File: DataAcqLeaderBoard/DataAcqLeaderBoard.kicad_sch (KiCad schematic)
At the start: 11 parts, among them SW1 UP, U1 PA1616S_GPS

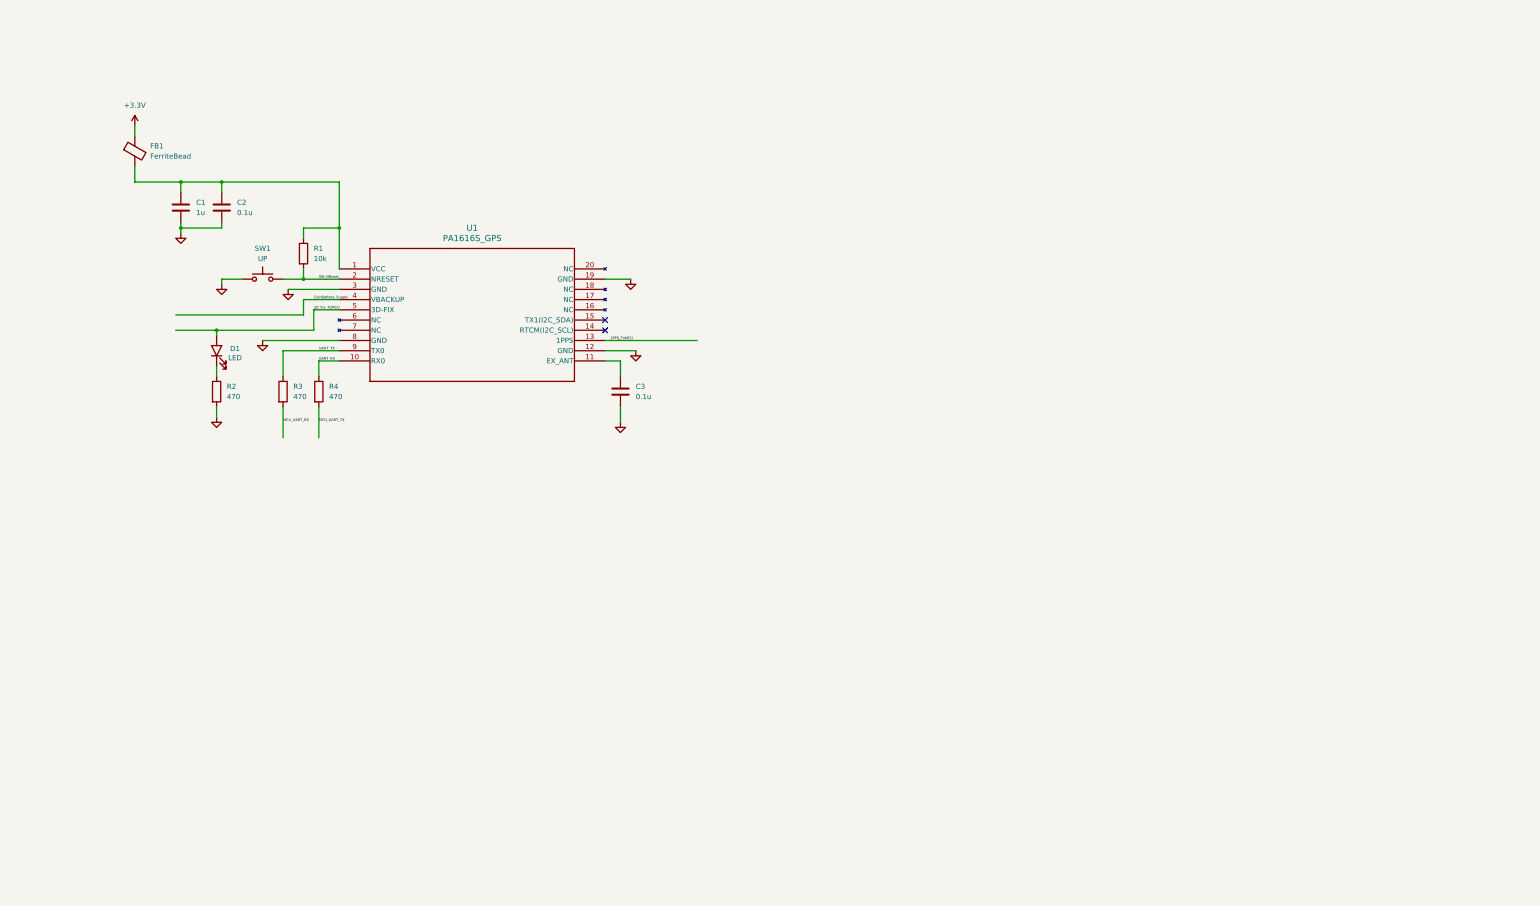
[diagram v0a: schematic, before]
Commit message: Added XBee RF Module
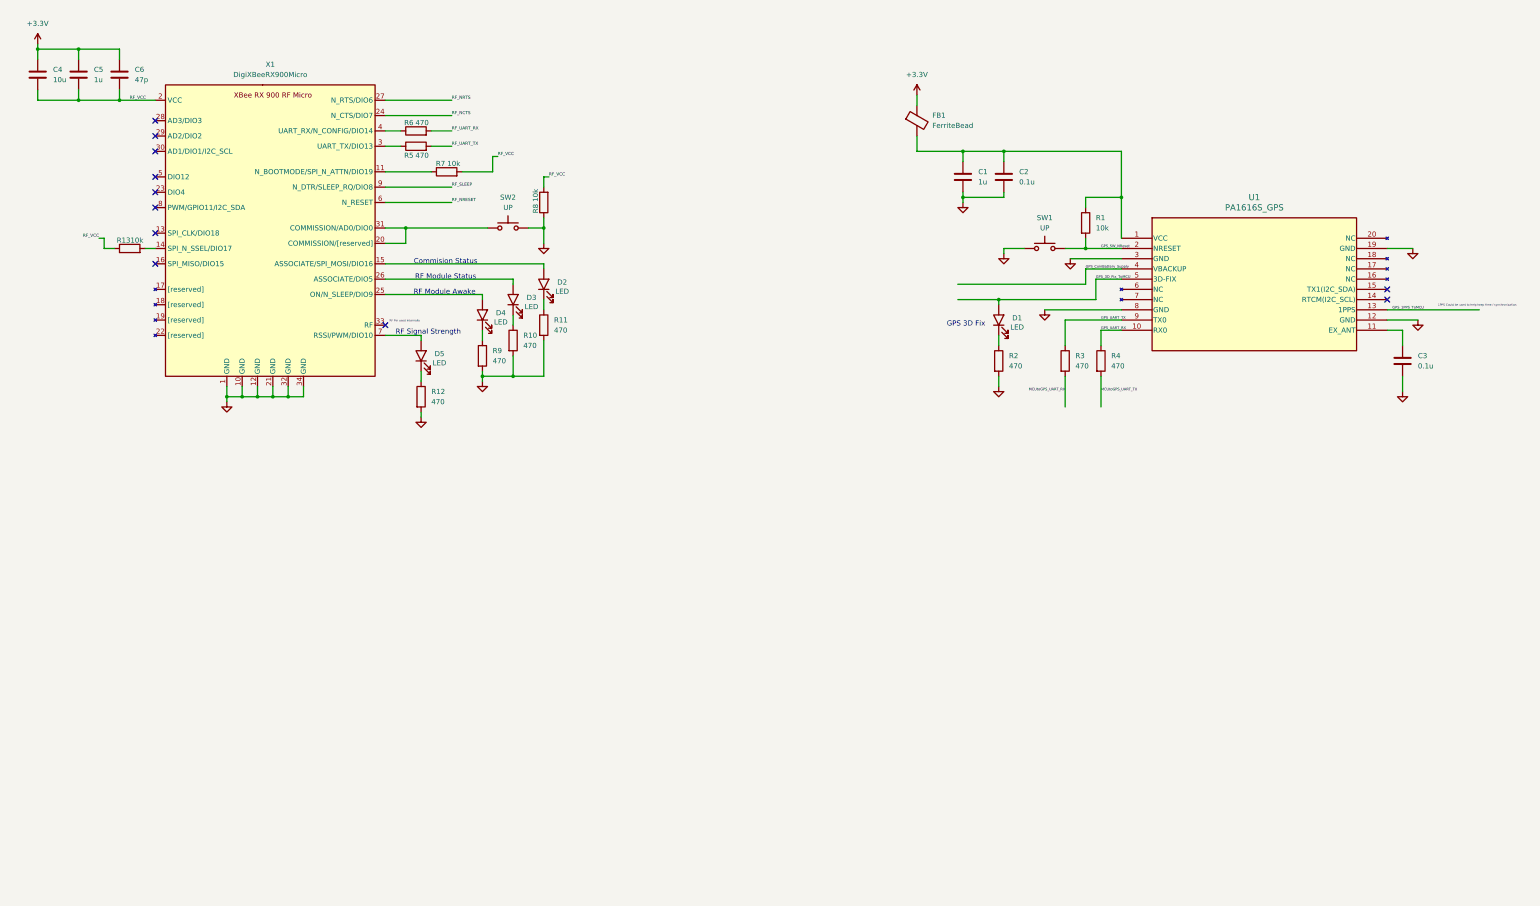
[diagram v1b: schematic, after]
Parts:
- added C4: 10u, ECE319K:C_Axial_200mil, symbol ECE319K:C
- added C5: 1u, ECE319K:C_Axial_200mil, symbol ECE319K:C
- added C6: 47p, ECE319K:C_Axial_200mil, symbol ECE319K:C
- added D2, D3, D4, D5: LED, ECE319K:LED_D5.0mm, symbol ECE319K:LED
- added R10, R11, R12, R5, R6, R9: 470, symbol Device:R
- added R13, R7, R8: 10k, symbol Device:R
- added SW2: UP, ECE319K:SW_PUSH_6mm, symbol ECE319K:SW_Push
- added X1: DigiXBeeRX900Micro, symbol DataAcqLeaderBoard-SchematicSymbols:DigiXBeeRX900Micro
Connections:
- net +3.3V: now also C4.1, C5.1, C6.1
- net GND: now also R10.2, R11.2, R12.2, R8.1, R9.2, SW2.2, X1.1 (GND), X1.10 (GND), X1.12 (GND), X1.21 (GND), X1.32 (GND), X1.34 (GND)
- net 1PPS_ToMCU renamed GPS_1PPS_ToMCU
- net 3D_Fix_ToMCU renamed GPS_3D_Fix_ToMCU
- net CoinBattery_Supply renamed GPS_CoinBattery_Supply
- net MCU_UART_RX renamed MCUtoGPS_UART_RX
- net MCU_UART_TX renamed MCUtoGPS_UART_TX
- net SW_NReset renamed GPS_SW_NReset
- net UART_RX renamed GPS_UART_RX
- net UART_TX renamed GPS_UART_TX
- new net: D2.1 (K), R11.1
- new net: D3.1 (K), R10.1
- new net: D3.2 (A), X1.26 (ASSOCIATE/DIO5)
- new net: D5.1 (K), R12.1
- new net: SW2.1, X1.20 (COMMISSION/[reserved]), X1.31 (COMMISSION/AD0/DIO0)
- new net: R6.1, X1.4 (UART_RX/N_CONFIG/DIO14)
- new net: R7.1, X1.11 (N_BOOTMODE/SPI_N_ATTN/DIO19)
- new net: R13.2, X1.14 (SPI_N_SSEL/DIO17)
- new net: D2.2 (A), X1.15 (ASSOCIATE/SPI_MOSI/DIO16)
- new net: D4.2 (A), X1.25 (ON/N_SLEEP/DIO9)
- new net: R5.1, X1.3 (UART_TX/DIO13)
- new net: D5.2 (A), X1.7 (RSSI/PWM/DIO10)
- new net: D4.1 (K), R9.1
- new net RF_NCTS: X1.24 (N_CTS/DIO7)
- new net RF_NRESET: X1.6 (N_RESET)
- new net RF_NRTS: X1.27 (N_RTS/DIO6)
- new net RF_SLEEP: X1.9 (N_DTR/SLEEP_RQ/DIO8)
- new net RF_UART_RX: R6.2
- new net RF_UART_TX: R5.2
- new net RF_VCC: C4.2, C5.2, C6.2, R13.1, R7.2, R8.2, X1.2 (VCC)
- no-connect marks 2 -> 11
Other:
- note added: "1PPS Could be used to help keep time / synchronization"
- note added: "Commision Status"
- note added: "GPS 3D Fix"
- note added: "RF Module Awake"
- note added: "RF Module Status"
- note added: "RF Pin used internally"
- note added: "RF Signal Strength"
- moved on the sheet: C1, C2, C3, D1, FB1, R1, R2, R3, R4, SW1

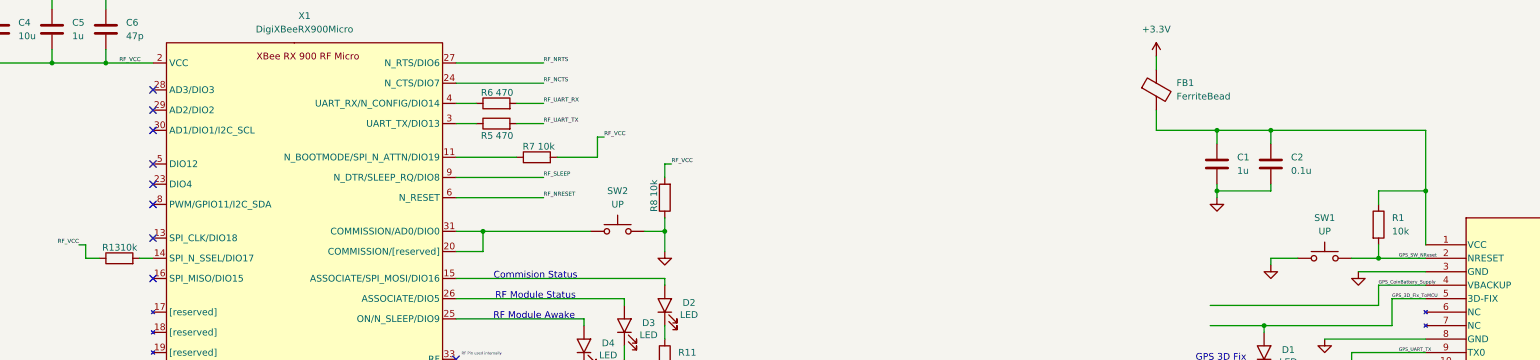
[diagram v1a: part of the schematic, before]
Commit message: Fixed RF Module's push buttons
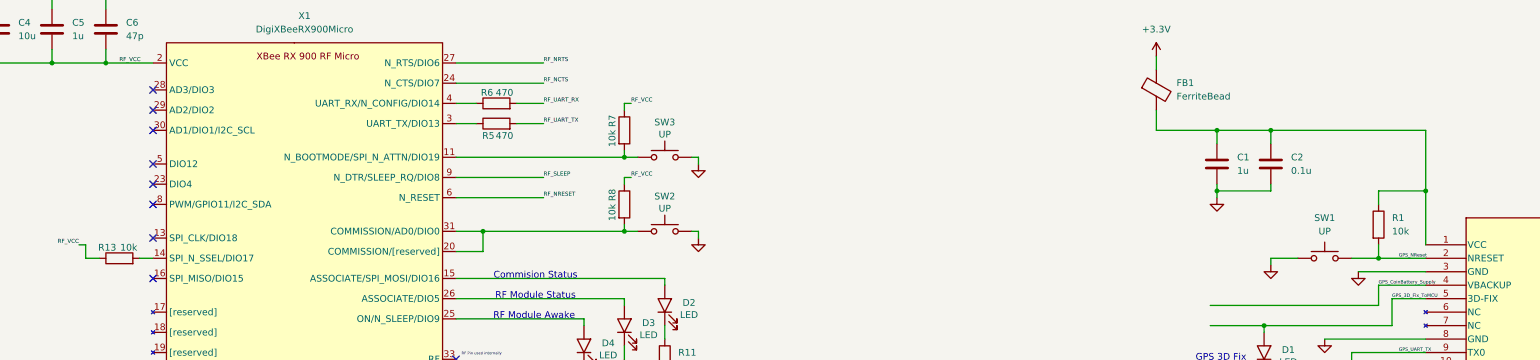
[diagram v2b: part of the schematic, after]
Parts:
- added SW3: UP, ECE319K:SW_PUSH_6mm, symbol ECE319K:SW_Push
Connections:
- net GND: now also SW3.2; no longer R8.1
- net RF_VCC: now also R7.1, R8.1; no longer R7.2, R8.2
- net at SW2.1, X1.20 (COMMISSION/[reserved]), X1.31 (COMMISSION/AD0/DIO0): now also R8.2
- net at X1.11 (N_BOOTMODE/SPI_N_ATTN/DIO19): now also R7.2, SW3.1; no longer R7.1
- net GPS_SW_NReset renamed GPS_NReset

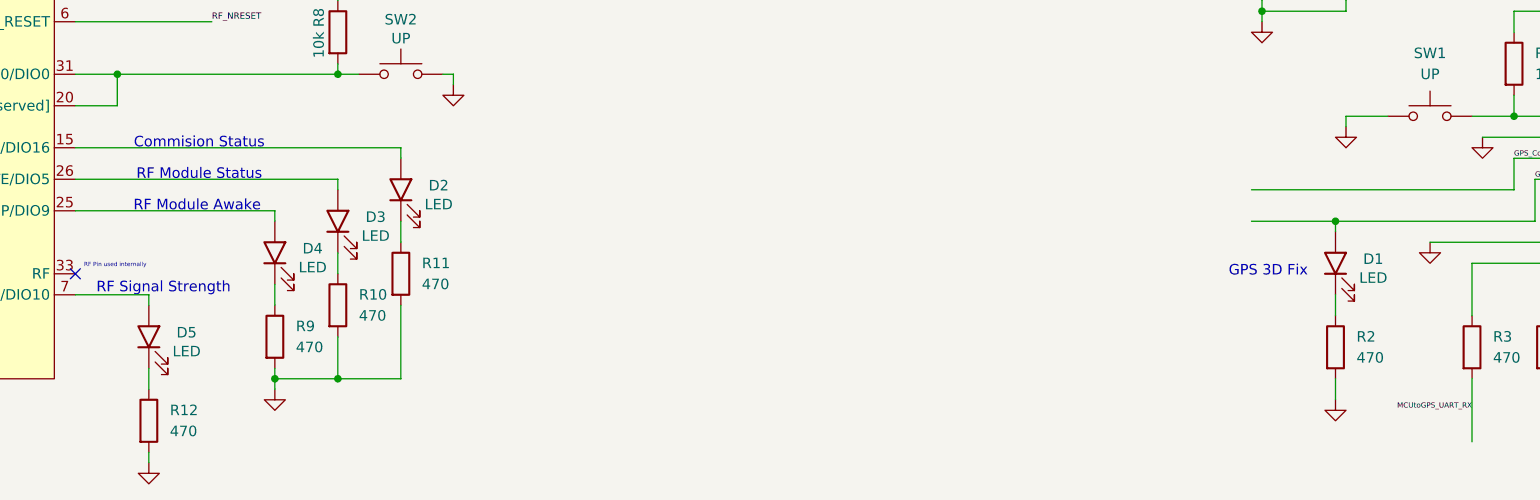
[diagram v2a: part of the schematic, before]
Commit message: Fixed project paths and added .gitignore
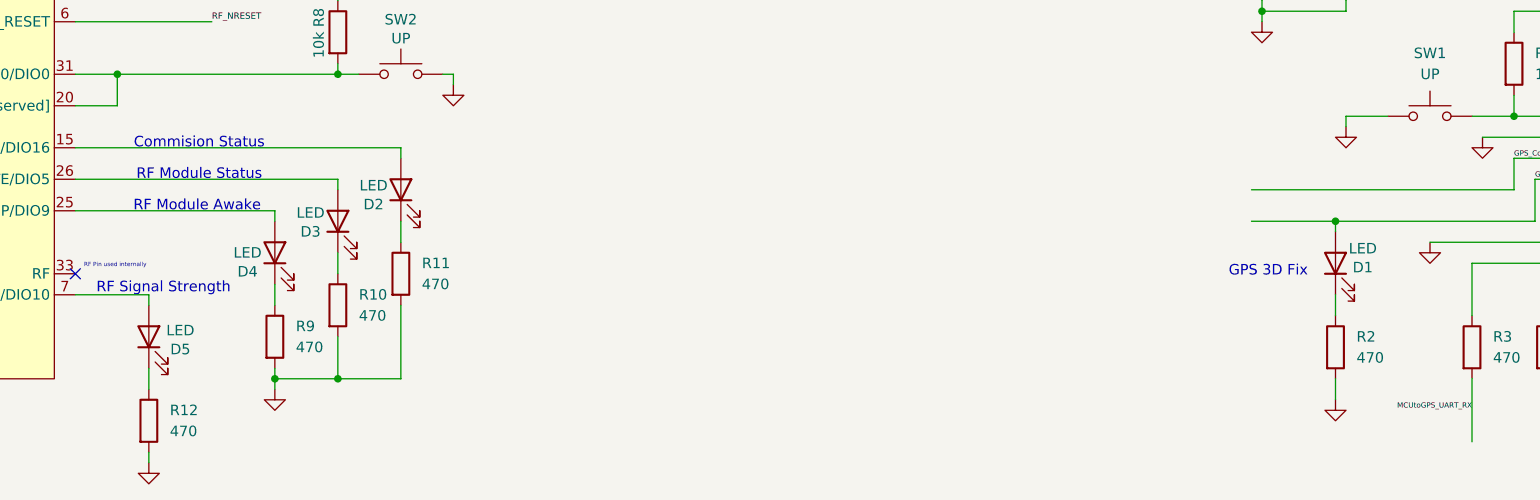
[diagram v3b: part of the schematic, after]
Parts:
- C4, C5, C6: footprint ECE319K:C_Axial_200mil -> (none); symbol ECE319K:C -> Device:C
- D1, D2, D3, D4, D5: footprint ECE319K:LED_D5.0mm -> (none); symbol ECE319K:LED -> Device:LED
- SW1, SW2, SW3: footprint ECE319K:SW_PUSH_6mm -> (none); symbol ECE319K:SW_Push -> Switch:SW_Push
- U1: footprint PA1616S_ADA -> PA_1616S_GPS:PA1616S_ADA
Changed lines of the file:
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@@
 	(wire
 		(pts
+			(xy 144.78 96.52) (xy 144.78 99.06)
+		)
+		(stroke
+			(width 0)
+			(type default)
+		)
+	)
+	(wire
+		(pts
 			(xy 77.47 114.3) (xy 77.47 116.84)
 		)
@@
 	(wire
 		(pts
-			(xy 144.78 96.52) (xy 144.78 99.06)
-		)
-		(stroke
-			(width 0)
-			(type default)
-		)
-	)
-	(wire
-		(pts
 			(xy 81.28 114.3) (xy 81.28 116.84)
 		)
@@
 	)
 	(symbol
-		(lib_id "ECE319K:LED")
-		(at 146.05 92.71 0)
+		(lib_id "Device:LED")
+		(at 144.78 92.71 90)
 		(unit 1)
 		(exclude_from_sim no)
@@
 		(dnp no)
 		(property "Reference" "D3"
-			(at 149.352 92.202 0)
+			(at 141.478 93.98 90)
 			(effects
 				(font
@@
 		)
 		(property "Value" "LED"
-			(at 149.352 94.488 0)
+			(at 141.478 91.694 90)
 			(effects
 				(font
@@
 			)
 		)
-		(property "Footprint" "ECE319K:LED_D5.0mm"
-			(at 146.05 90.17 0)
+		(property "Footprint" ""
+			(at 142.24 92.71 0)
 			(effects
 				(font
@@
 			)
 		)
-		(property "Datasheet" "https://users.ece.utexas.edu/~valvano/mspm0/HLMP-4700.pdf"
-			(at 146.05 90.17 0)
+		(property "Datasheet" ""
+			(at 142.24 92.71 0)
 			(effects
 				(font
@@
 		)
 		(property "Description" "Light emitting diode"
-			(at 146.05 92.71 0)
+			(at 144.78 92.71 0)
 			(effects
 				(font
@@
 			)
 		)
-		(property "Footprint" "PA1616S_ADA"
-			(at 329.438 64.262 0)
+		(property "Footprint" "PA_1616S_GPS:PA1616S_ADA"
+			(at 308.864 59.944 0)
 			(effects
 				(font
@@
 			)
 		)
-		(property "Datasheet" "790"
-			(at 329.184 67.056 0)
+		(property "Datasheet" "https://cdn-shop.adafruit.com/product-files/746/CD+PA1616S+Datasheet.v03.pdf"
+			(at 335.788 63.246 0)
 			(effects
 				(font
@@
 	)
 	(symbol
-		(lib_id "ECE319K:LED")
-		(at 266.7 97.79 0)
+		(lib_id "Device:LED")
+		(at 265.43 97.79 90)
 		(unit 1)
 		(exclude_from_sim no)
@@
 		(dnp no)
 		(property "Reference" "D1"
-			(at 270.002 97.282 0)
+			(at 268.732 98.298 90)
 			(effects
 				(font
@@
 		)
 		(property "Value" "LED"
-			(at 270.002 99.568 0)
+			(at 268.732 96.012 90)
 			(effects
 				(font
@@
 			)
 		)
-		(property "Footprint" "ECE319K:LED_D5.0mm"
-			(at 266.7 95.25 0)
+		(property "Footprint" ""
+			(at 262.89 97.79 0)
 			(effects
 				(font
@@
 			)
 		)
-		(property "Datasheet" "https://users.ece.utexas.edu/~valvano/mspm0/HLMP-4700.pdf"
-			(at 266.7 95.25 0)
+		(property "Datasheet" ""
+			(at 262.89 97.79 0)
 			(effects
 				(font
@@
 		)
 		(property "Description" "Light emitting diode"
-			(at 266.7 97.79 0)
+			(at 265.43 97.79 0)
 			(effects
 				(font
@@
 	)
 	(symbol
-		(lib_id "ECE319K:C")
+		(lib_id "Device:C")
 		(at 46.99 36.83 0)
 		(unit 1)
@@
 			)
 		)
-		(property "Footprint" "ECE319K:C_Axial_200mil"
+		(property "Footprint" ""
 			(at 47.9552 40.64 0)
 			(effects
@@
 	)
 	(symbol
-		(lib_id "ECE319K:LED")
-		(at 138.43 96.52 0)
+		(lib_id "Device:LED")
+		(at 137.16 96.52 90)
 		(unit 1)
 		(exclude_from_sim no)
@@
 		(dnp no)
 		(property "Reference" "D4"
-			(at 141.732 96.012 0)
+			(at 133.858 98.806 90)
 			(effects
 				(font
@@
 		)
 		(property "Value" "LED"
-			(at 141.732 98.298 0)
+			(at 133.858 96.52 90)
 			(effects
 				(font
@@
 			)
 		)
-		(property "Footprint" "ECE319K:LED_D5.0mm"
-			(at 138.43 93.98 0)
+		(property "Footprint" ""
+			(at 134.62 96.52 0)
 			(effects
 				(font
@@
 			)
 		)
-		(property "Datasheet" "https://users.ece.utexas.edu/~valvano/mspm0/HLMP-4700.pdf"
-			(at 138.43 93.98 0)
+		(property "Datasheet" ""
+			(at 134.62 96.52 0)
 			(effects
 				(font
@@
 		)
 		(property "Description" "Light emitting diode"
-			(at 138.43 96.52 0)
+			(at 137.16 96.52 0)
 			(effects
 				(font
@@
 	)
 	(symbol
-		(lib_id "ECE319K:LED")
-		(at 123.19 106.68 0)
+		(lib_id "Device:LED")
+		(at 121.92 106.68 90)
 		(unit 1)
 		(exclude_from_sim no)
@@
 		(dnp no)
 		(property "Reference" "D5"
-			(at 126.492 106.172 0)
+			(at 125.73 108.204 90)
 			(effects
 				(font
@@
 		)
 		(property "Value" "LED"
-			(at 126.492 108.458 0)
+			(at 125.73 105.918 90)
 			(effects
 				(font
@@
 			)
 		)
-		(property "Footprint" "ECE319K:LED_D5.0mm"
-			(at 123.19 104.14 0)
+		(property "Footprint" ""
+			(at 119.38 106.68 0)
 			(effects
 				(font
@@
 			)
 		)
-		(property "Datasheet" "https://users.ece.utexas.edu/~valvano/mspm0/HLMP-4700.pdf"
-			(at 123.19 104.14 0)
+		(property "Datasheet" ""
+			(at 119.38 106.68 0)
 			(effects
 				(font
@@
 		)
 		(property "Description" "Light emitting diode"
-			(at 123.19 106.68 0)
+			(at 121.92 106.68 0)
 			(effects
 				(font
@@
 	)
 	(symbol
-		(lib_id "ECE319K:SW_Push")
+		(lib_id "Switch:SW_Push")
 		(at 276.86 80.01 0)
 		(unit 1)
@@
 			)
 		)
-		(property "Footprint" "ECE319K:SW_PUSH_6mm"
+		(property "Footprint" ""
 			(at 276.86 74.93 0)
 			(effects
@@
 			)
 		)
-		(property "Datasheet" "~"
+		(property "Datasheet" ""
 			(at 276.86 74.93 0)
 			(effects
@@
 	)
 	(symbol
-		(lib_id "ECE319K:LED")
-		(at 153.67 88.9 0)
+		(lib_id "Device:LED")
+		(at 152.4 88.9 90)
 		(unit 1)
 		(exclude_from_sim no)
@@
 		(dnp no)
 		(property "Reference" "D2"
-			(at 156.972 88.392 0)
+			(at 149.098 90.678 90)
 			(effects
 				(font
@@
 		)
 		(property "Value" "LED"
-			(at 156.972 90.678 0)
+			(at 149.098 88.392 90)
 			(effects
 				(font
@@
 			)
 		)
-		(property "Footprint" "ECE319K:LED_D5.0mm"
-			(at 153.67 86.36 0)
+		(property "Footprint" ""
+			(at 149.86 88.9 0)
 			(effects
 				(font
@@
 			)
 		)
-		(property "Datasheet" "https://users.ece.utexas.edu/~valvano/mspm0/HLMP-4700.pdf"
-			(at 153.67 86.36 0)
+		(property "Datasheet" ""
+			(at 149.86 88.9 0)
 			(effects
 				(font
@@
 		)
 		(property "Description" "Light emitting diode"
-			(at 153.67 88.9 0)
+			(at 152.4 88.9 0)
 			(effects
 				(font
@@
 	)
 	(symbol
-		(lib_id "ECE319K:C")
+		(lib_id "Device:C")
 		(at 36.83 36.83 0)
 		(unit 1)
@@
 			)
 		)
-		(property "Footprint" "ECE319K:C_Axial_200mil"
+		(property "Footprint" ""
 			(at 37.7952 40.64 0)
 			(effects
@@
 			)
 		)
-		(property "Datasheet" "~"
+		(property "Datasheet" ""
 			(at 36.83 36.83 0)
 			(effects
@@
 	)
 	(symbol
-		(lib_id "ECE319K:SW_Push")
+		(lib_id "Switch:SW_Push")
 		(at 152.4 74.93 0)
 		(unit 1)
@@
 			)
 		)
-		(property "Footprint" "ECE319K:SW_PUSH_6mm"
+		(property "Footprint" ""
 			(at 152.4 69.85 0)
 			(effects
@@
 	)
 	(symbol
-		(lib_id "ECE319K:SW_Push")
+		(lib_id "Switch:SW_Push")
 		(at 152.4 60.96 0)
 		(unit 1)
@@
 			)
 		)
-		(property "Footprint" "ECE319K:SW_PUSH_6mm"
+		(property "Footprint" ""
 			(at 152.4 55.88 0)
 			(effects
@@
 	)
 	(symbol
-		(lib_id "ECE319K:C")
+		(lib_id "Device:C")
 		(at 26.67 36.83 0)
 		(unit 1)
@@
 			)
 		)
-		(property "Footprint" "ECE319K:C_Axial_200mil"
+		(property "Footprint" ""
 			(at 27.6352 40.64 0)
 			(effects

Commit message: Actually fixed the symbol, footprint paths
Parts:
- U1: footprint PA_1616S_GPS:PA1616S_ADA -> DataAcqLeaderBoard-Footprints:PA1616S_ADA; symbol PA1616S_GPS:790 -> DataAcqLeaderBoard-Symbols:PA1616S_GPS
- X1: symbol DataAcqLeaderBoard-SchematicSymbols:DigiXBeeRX900Micro -> DataAcqLeaderBoard-Symbols:DigiXBeeRX900Micro
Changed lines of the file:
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@@
 	)
 	(symbol
-		(lib_id "PA1616S_GPS:790")
+		(lib_id "DataAcqLeaderBoard-Symbols:PA1616S_GPS")
 		(at 295.91 77.47 0)
 		(unit 1)
@@
 			)
 		)
-		(property "Footprint" "PA_1616S_GPS:PA1616S_ADA"
-			(at 308.864 59.944 0)
+		(property "Footprint" "DataAcqLeaderBoard-Footprints:PA1616S_ADA"
+			(at 326.898 63.5 0)
 			(effects
 				(font
@@
 		)
 		(property "Datasheet" "https://cdn-shop.adafruit.com/product-files/746/CD+PA1616S+Datasheet.v03.pdf"
-			(at 335.788 63.246 0)
+			(at 345.44 67.056 0)
 			(effects
 				(font
@@
 	)
 	(symbol
-		(lib_id "DataAcqLeaderBoard-SchematicSymbols:DigiXBeeRX900Micro")
+		(lib_id "DataAcqLeaderBoard-Symbols:DigiXBeeRX900Micro")
 		(at 39.37 130.81 0)
 		(unit 1)
